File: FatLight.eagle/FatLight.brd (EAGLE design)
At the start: 75 x 100 mm, 27 parts, among them J1 12V, Q1 IRF540, Q2 IRF540, Q3 IRF540, Q4 16MHz, U1 ATMEGA328P-PU

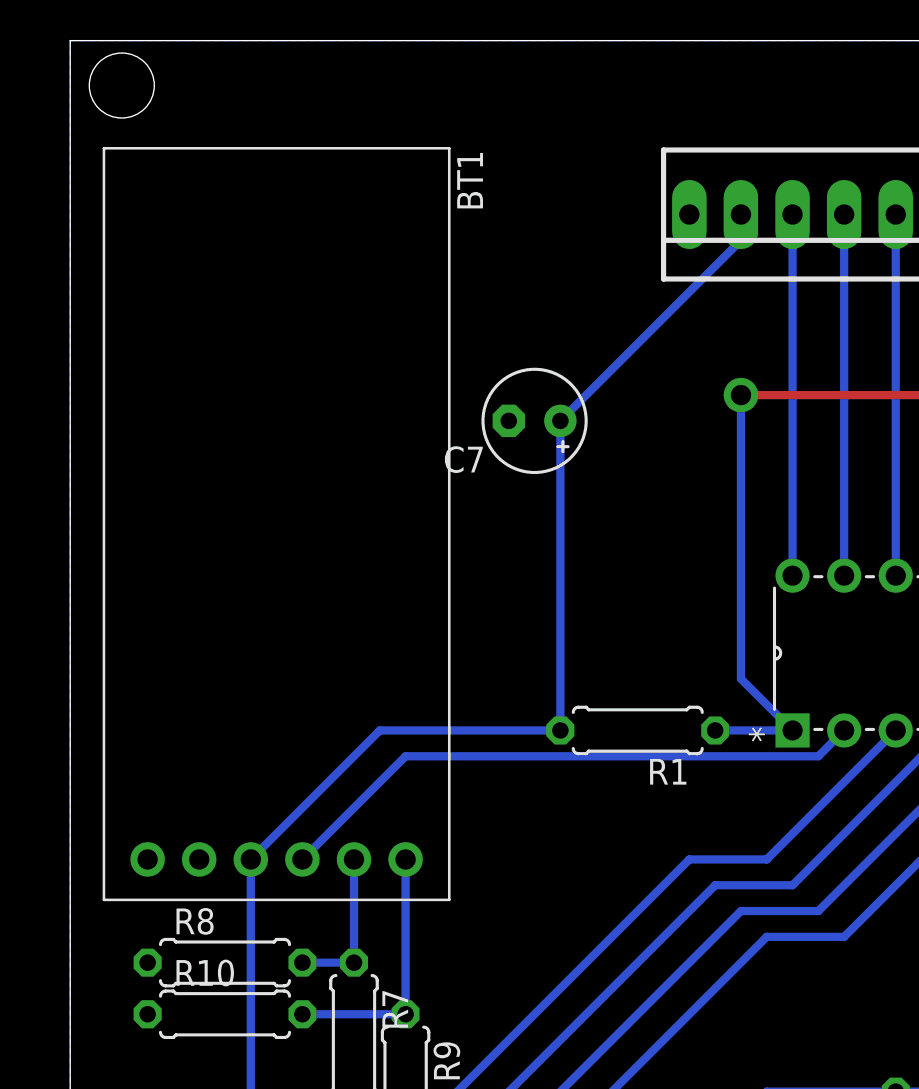
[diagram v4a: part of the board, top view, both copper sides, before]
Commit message: Updated Board and Schmeatics so either of two different HC-05 module types can be fitted. Bugfixes.
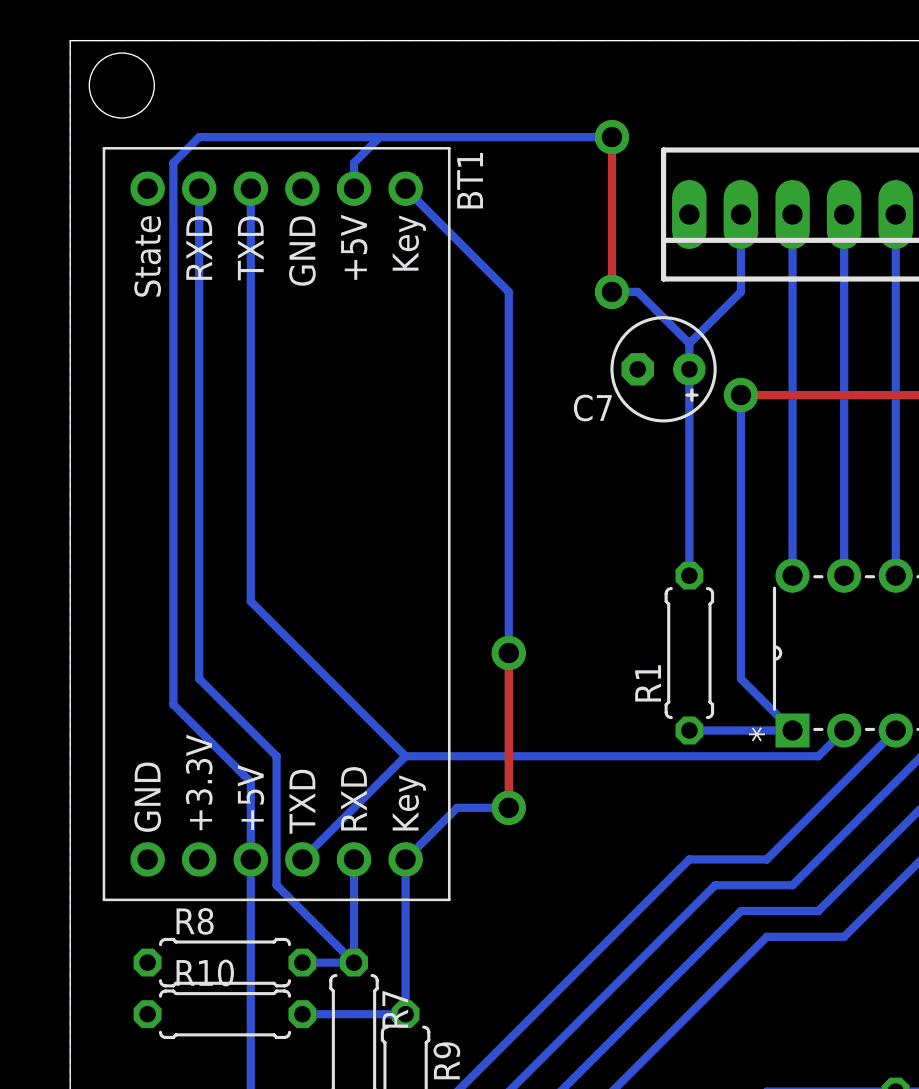
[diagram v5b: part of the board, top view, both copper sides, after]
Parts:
- moved C7 6.84 mm to (29.2, 83.8)
- moved R1 4.58 mm to (30.5, 69.8), turned to 90 degrees
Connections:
- net +5V: now also BT1.+5V1
- net GND: now also BT1.GND1
- net N$3: now also BT1.KEY1
- net N$4: now also BT1.RXD1
- net RXD_MCU: now also BT1.TXD1
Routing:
- net +5V: track 165.9 -> 211.3 mm, vias 0 -> 2
- net N$4: track 7.62 -> 48.9 mm
- net N$3: track 12.7 -> 51.4 mm, vias 0 -> 2
- net RXD_MCU: track 29.3 -> 60.4 mm
- net RESET: track 60.7 -> 62.0 mm
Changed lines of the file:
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@@
 <attribute name="OC_FARNELL" value="1667008" x="55.88" y="55.88" size="1.778" layer="27" rot="R90" display="off"/>
 </element>
-<element name="R1" library="rcl" package="0207/7" value="10k" x="27.94" y="66.04" rot="R180"/>
+<element name="R1" library="rcl" package="0207/7" value="10k" x="30.48" y="69.85" rot="R90"/>
 <element name="R10" library="rcl" package="0207/7" value="20k" x="7.62" y="52.07"/>
 <element name="R2" library="rcl" package="0207/7" value="10k" x="60.96" y="38.1" rot="R270"/>
@@
 <attribute name="OC_FARNELL" value="1715487" x="68.58" y="73.66" size="1.778" layer="27" rot="R90" display="off"/>
 </element>
-<element name="C7" library="rcl" package="E2,5-5" value="100µF" x="22.86" y="81.28" rot="R180"/>
+<element name="C7" library="rcl" package="E2,5-5" value="100µF" x="29.21" y="83.82" rot="R180"/>
 <element name="C8" library="rcl" package="C025-025X050" value="100nF" x="53.34" y="86.36" rot="R90"/>
 </elements>
@@
 <contactref element="C1" pad="2"/>
 <contactref element="C8" pad="2"/>
+<contactref element="BT1" pad="GND1"/>
 </signal>
 <signal name="+5V">
@@
 <wire x1="12.7" y1="41.91" x2="8.89" y2="45.72" width="0.4064" layer="16"/>
 <wire x1="8.89" y1="45.72" x2="8.89" y2="59.69" width="0.4064" layer="16"/>
-<wire x1="8.89" y1="59.69" x2="15.24" y2="66.04" width="0.4064" layer="16"/>
-<wire x1="15.24" y1="66.04" x2="24.13" y2="66.04" width="0.4064" layer="16"/>
 <wire x1="60.96" y1="91.44" x2="58.42" y2="91.44" width="0.4064" layer="16"/>
 <wire x1="58.42" y1="91.44" x2="55.88" y2="88.9" width="0.4064" layer="16"/>
 <wire x1="55.88" y1="88.9" x2="55.88" y2="78.74" width="0.4064" layer="16"/>
-<wire x1="24.13" y1="81.28" x2="24.13" y2="66.04" width="0.4064" layer="16"/>
+<wire x1="30.48" y1="83.82" x2="30.48" y2="73.66" width="0.4064" layer="16"/>
 <wire x1="15.24" y1="36.83" x2="15.24" y2="39.37" width="0.4064" layer="16"/>
 <wire x1="44.45" y1="64.77" x2="44.45" y2="67.31" width="0.4064" layer="16"/>
 <wire x1="44.45" y1="67.31" x2="46.99" y2="69.85" width="0.4064" layer="16"/>
 <wire x1="46.99" y1="69.85" x2="53.34" y2="69.85" width="0.4064" layer="16"/>
-<wire x1="33.02" y1="91.44" x2="33.02" y2="90.17" width="0.4064" layer="16"/>
-<wire x1="33.02" y1="90.17" x2="24.13" y2="81.28" width="0.4064" layer="16"/>
+<wire x1="30.48" y1="85.09" x2="30.48" y2="83.82" width="0.4064" layer="16"/>
 <wire x1="44.45" y1="64.77" x2="36.83" y2="57.15" width="0.4064" layer="16"/>
 <wire x1="36.83" y1="57.15" x2="33.02" y2="57.15" width="0.4064" layer="16"/>
@@
 <wire x1="33.02" y1="57.15" x2="15.24" y2="39.37" width="0.4064" layer="16"/>
 <contactref element="C7" pad="+"/>
+<contactref element="BT1" pad="+5V1"/>
+<wire x1="13.97" y1="92.71" x2="13.97" y2="93.98" width="0.4064" layer="16"/>
+<wire x1="13.97" y1="93.98" x2="15.24" y2="95.25" width="0.4064" layer="16"/>
+<wire x1="8.89" y1="59.69" x2="8.89" y2="63.5" width="0.4064" layer="16"/>
+<wire x1="8.89" y1="63.5" x2="5.08" y2="67.31" width="0.4064" layer="16"/>
+<wire x1="5.08" y1="67.31" x2="5.08" y2="93.98" width="0.4064" layer="16"/>
+<wire x1="5.08" y1="93.98" x2="6.35" y2="95.25" width="0.4064" layer="16"/>
+<wire x1="6.35" y1="95.25" x2="15.24" y2="95.25" width="0.4064" layer="16"/>
+<wire x1="33.02" y1="91.44" x2="33.02" y2="87.63" width="0.4064" layer="16"/>
+<wire x1="33.02" y1="87.63" x2="30.48" y2="85.09" width="0.4064" layer="16"/>
+<wire x1="15.24" y1="95.25" x2="26.67" y2="95.25" width="0.4064" layer="16"/>
+<via x="26.67" y="95.25" extent="1-16" drill="1"/>
+<wire x1="26.67" y1="95.25" x2="26.67" y2="87.63" width="0.4064" layer="1"/>
+<via x="26.67" y="87.63" extent="1-16" drill="1"/>
+<wire x1="26.67" y1="87.63" x2="27.94" y2="87.63" width="0.4064" layer="16"/>
+<wire x1="27.94" y1="87.63" x2="30.48" y2="85.09" width="0.4064" layer="16"/>
 </signal>
 <signal name="RESET">
@@
 <wire x1="33.02" y1="82.55" x2="33.02" y2="68.58" width="0.4064" layer="16"/>
 <wire x1="33.02" y1="68.58" x2="35.56" y2="66.04" width="0.4064" layer="16"/>
-<wire x1="35.56" y1="66.04" x2="31.75" y2="66.04" width="0.4064" layer="16"/>
+<wire x1="35.56" y1="66.04" x2="30.48" y2="66.04" width="0.4064" layer="16"/>
 </signal>
 <signal name="PWM_RED">
@@
 <wire x1="38.1" y1="66.04" x2="36.83" y2="64.77" width="0.4064" layer="16"/>
 <wire x1="36.83" y1="64.77" x2="16.51" y2="64.77" width="0.4064" layer="16"/>
+<contactref element="BT1" pad="TXD1"/>
+<wire x1="8.89" y1="92.71" x2="8.89" y2="72.39" width="0.4064" layer="16"/>
+<wire x1="8.89" y1="72.39" x2="16.51" y2="64.77" width="0.4064" layer="16"/>
 </signal>
 <signal name="TXD_MCU">
@@
 <wire x1="11.43" y1="52.07" x2="16.51" y2="52.07" width="0.4064" layer="16"/>
 <wire x1="16.51" y1="59.69" x2="16.51" y2="52.07" width="0.4064" layer="16"/>
+<contactref element="BT1" pad="KEY1"/>
+<wire x1="16.51" y1="59.69" x2="19.05" y2="62.23" width="0.4064" layer="16"/>
+<wire x1="19.05" y1="62.23" x2="21.59" y2="62.23" width="0.4064" layer="16"/>
+<via x="21.59" y="62.23" extent="1-16" drill="1"/>
+<wire x1="21.59" y1="62.23" x2="21.59" y2="69.85" width="0.4064" layer="1"/>
+<via x="21.59" y="69.85" extent="1-16" drill="1"/>
+<wire x1="21.59" y1="69.85" x2="21.59" y2="87.63" width="0.4064" layer="16"/>
+<wire x1="21.59" y1="87.63" x2="16.51" y2="92.71" width="0.4064" layer="16"/>
 </signal>
 <signal name="N$4">
@@
 <wire x1="11.43" y1="54.61" x2="13.97" y2="54.61" width="0.4064" layer="16"/>
 <wire x1="13.97" y1="59.69" x2="13.97" y2="54.61" width="0.4064" layer="16"/>
+<contactref element="BT1" pad="RXD1"/>
+<wire x1="6.35" y1="92.71" x2="6.35" y2="68.58" width="0.4064" layer="16"/>
+<wire x1="10.16" y1="64.77" x2="10.16" y2="58.42" width="0.4064" layer="16"/>
+<wire x1="10.16" y1="58.42" x2="13.97" y2="54.61" width="0.4064" layer="16"/>
+<wire x1="6.35" y1="68.58" x2="10.16" y2="64.77" width="0.4064" layer="16"/>
 </signal>
 <signal name="N$5">

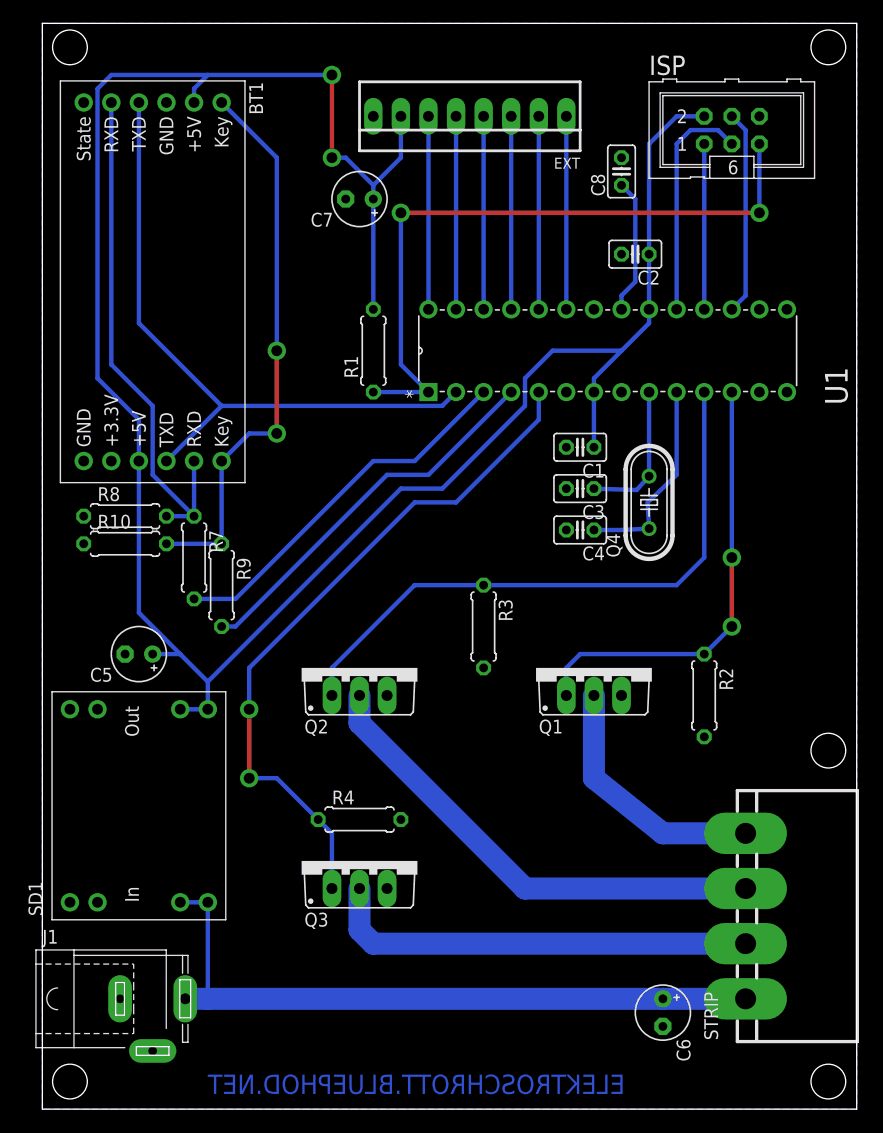
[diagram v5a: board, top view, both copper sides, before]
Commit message: Cap setting for random values added, optimized board layout.
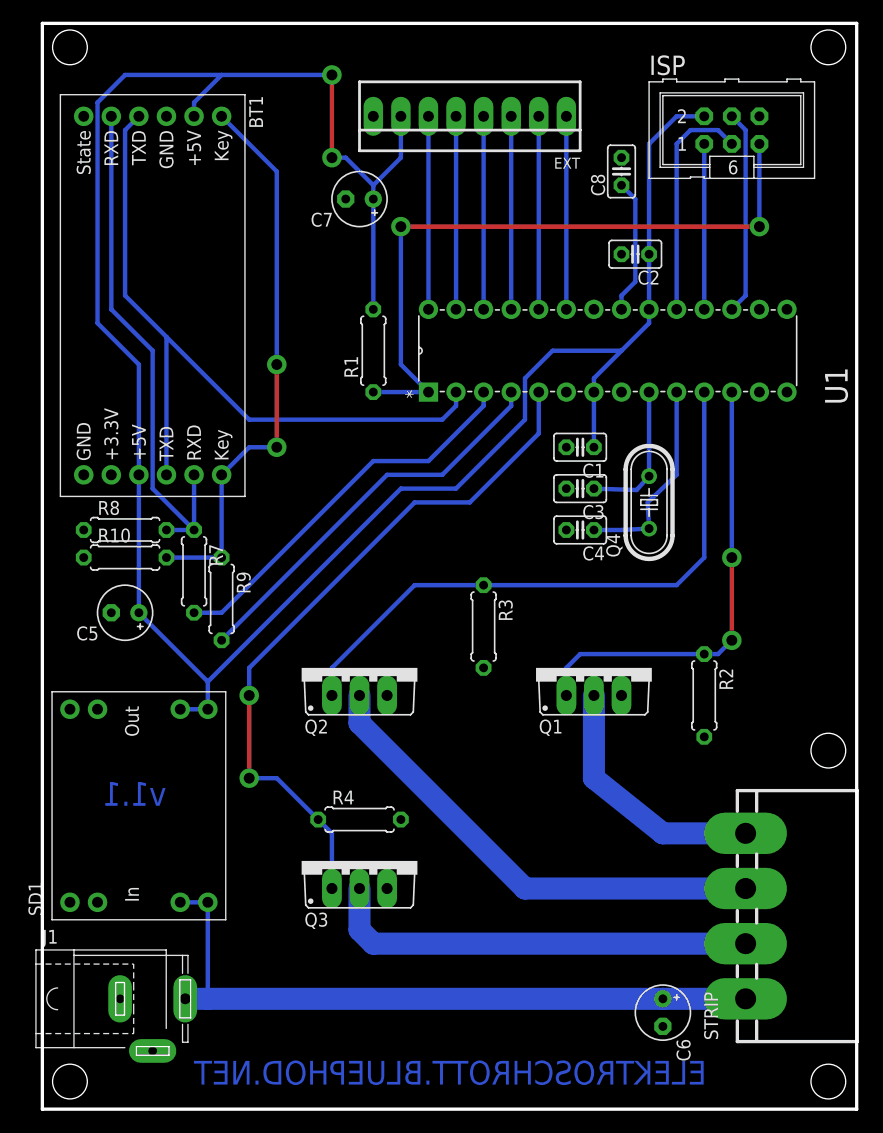
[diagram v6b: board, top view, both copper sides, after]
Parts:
- moved C5 4.02 mm to (7.62, 45.7)
- moved R10 1.27 mm to (7.62, 50.8)
- moved BT1 1.27 mm to (10.2, 74.9)
- moved R7 1.27 mm to (14.0, 49.5)
- moved R8 1.27 mm to (7.62, 53.3)
- moved R9 1.27 mm to (16.5, 47.0)
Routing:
- net RXD_MCU: track 60.4 -> 66.7 mm
- net TXD_MCU: track 34.6 -> 35.8 mm
- net KEY: track 35.6 -> 36.9 mm
- net +5V: track 211.3 -> 210.6 mm
- net PWM_RED: track 40.9 -> 41.7 mm
- net PWM_BLU: track 63.6 -> 64.4 mm
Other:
- board text added: "v1.1"

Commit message: Fixed the dimensions of the d-sun step-down module.
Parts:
- SD1: value STEP-DOWN -> D-SUN-STEPDOWN
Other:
- outline, holes or cut-outs redrawn
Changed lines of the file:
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@@
 <grid distance="0.05" unitdist="inch" unit="inch" style="lines" multiple="1" display="yes" altdistance="0.025" altunitdist="inch" altunit="inch"/>
 <layers>
-<layer number="1" name="Top" color="4" fill="1" visible="yes" active="yes"/>
+<layer number="1" name="Top" color="4" fill="1" visible="no" active="yes"/>
 <layer number="2" name="Route2" color="1" fill="3" visible="no" active="no"/>
 <layer number="3" name="Route3" color="4" fill="3" visible="no" active="no"/>
@@
 <layer number="17" name="Pads" color="2" fill="1" visible="yes" active="yes"/>
 <layer number="18" name="Vias" color="2" fill="1" visible="yes" active="yes"/>
-<layer number="19" name="Unrouted" color="6" fill="1" visible="yes" active="yes"/>
+<layer number="19" name="Unrouted" color="6" fill="1" visible="no" active="yes"/>
 <layer number="20" name="Dimension" color="15" fill="1" visible="yes" active="yes"/>
-<layer number="21" name="tPlace" color="7" fill="1" visible="yes" active="yes"/>
-<layer number="22" name="bPlace" color="7" fill="1" visible="yes" active="yes"/>
-<layer number="23" name="tOrigins" color="15" fill="1" visible="yes" active="yes"/>
-<layer number="24" name="bOrigins" color="15" fill="1" visible="yes" active="yes"/>
+<layer number="21" name="tPlace" color="7" fill="1" visible="no" active="yes"/>
+<layer number="22" name="bPlace" color="7" fill="1" visible="no" active="yes"/>
+<layer number="23" name="tOrigins" color="15" fill="1" visible="no" active="yes"/>
+<layer number="24" name="bOrigins" color="15" fill="1" visible="no" active="yes"/>
 <layer number="25" name="tNames" color="7" fill="1" visible="no" active="yes"/>
 <layer number="26" name="bNames" color="7" fill="1" visible="no" active="yes"/>
@@
 <layer number="46" name="Milling" color="3" fill="1" visible="no" active="yes"/>
 <layer number="47" name="Measures" color="7" fill="1" visible="no" active="yes"/>
-<layer number="48" name="Document" color="7" fill="1" visible="yes" active="yes"/>
+<layer number="48" name="Document" color="7" fill="1" visible="no" active="yes"/>
 <layer number="49" name="Reference" color="7" fill="1" visible="no" active="yes"/>
 <layer number="51" name="tDocu" color="7" fill="1" visible="no" active="yes"/>
@@
 <text x="13.97" y="4.445" size="2.1844" layer="16" rot="MR180">ELEKTROSCHROTT.BLUEPHOD.NET</text>
 <text x="11.43" y="27.94" size="2.1844" layer="16" rot="MR0">v1.1</text>
+<circle x="2.54" y="97.79" radius="1.6" width="0.127" layer="20"/>
+<circle x="72.39" y="97.79" radius="1.6" width="0.127" layer="20"/>
+<circle x="72.39" y="33.02" radius="1.6" width="0.127" layer="20"/>
+<circle x="72.39" y="2.54" radius="1.6" width="0.127" layer="20"/>
+<circle x="2.54" y="2.54" radius="1.6" width="0.127" layer="20"/>
 </plain>
 <attributes>
@@
 <param name="msMicroVia" value="9.99mm"/>
 <param name="msBlindViaRatio" value="0.5"/>
-<param name="rvPadTop" value="0.4"/>
-<param name="rvPadInner" value="0.4"/>
-<param name="rvPadBottom" value="0.4"/>
-<param name="rvViaOuter" value="0.4"/>
-<param name="rvViaInner" value="0.4"/>
+<param name="rvPadTop" value="0.36"/>
+<param name="rvPadInner" value="0.36"/>
+<param name="rvPadBottom" value="0.36"/>
+<param name="rvViaOuter" value="0.36"/>
+<param name="rvViaInner" value="0.36"/>
 <param name="rvMicroViaOuter" value="0.25"/>
 <param name="rvMicroViaInner" value="0.25"/>
@@
 <element name="R8" library="rcl" package="0207/7" value="20k" x="7.62" y="53.34"/>
 <element name="R9" library="rcl" package="0207/7" value="10k" x="16.51" y="46.99" rot="R270"/>
-<element name="SD1" library="Zap-Powerconverters" package="STEPDOWN-21X16" value="STEP-DOWN" x="8.89" y="27.94" rot="R90"/>
+<element name="SD1" library="Zap-Powerconverters" package="STEPDOWN-21X16" value="D-SUN-STEPDOWN" x="8.89" y="27.94" rot="R90"/>
 <element name="STRIP" library="con-amp" package="FLOP-4V" value="" x="64.77" y="17.78" rot="R90"/>
 <element name="U1" library="Zap-Mikrocontroller" package="DIP254P762X457-28" value="ATMEGA328P-PU" x="68.58" y="73.66" rot="R90">
@@
 <wire x1="50.8" y1="66.04" x2="50.8" y2="60.96" width="0.4064" layer="16"/>
 <contactref element="SD1" pad="OUT+1"/>
-<wire x1="12.7" y1="36.83" x2="15.24" y2="36.83" width="0.4064" layer="16"/>
+<wire x1="12.7" y1="37.19" x2="15.24" y2="37.19" width="0.4064" layer="16"/>
 <wire x1="55.88" y1="73.66" x2="55.88" y2="72.39" width="0.4064" layer="16"/>
 <wire x1="55.88" y1="72.39" x2="53.34" y2="69.85" width="0.4064" layer="16"/>
@@
 <wire x1="26.67" y1="87.63" x2="27.94" y2="87.63" width="0.4064" layer="16"/>
 <wire x1="27.94" y1="87.63" x2="30.48" y2="85.09" width="0.4064" layer="16"/>
-<wire x1="15.24" y1="36.83" x2="15.24" y2="39.37" width="0.4064" layer="16"/>
+<wire x1="15.24" y1="37.19" x2="15.24" y2="39.37" width="0.4064" layer="16"/>
 <wire x1="8.89" y1="45.72" x2="15.24" y2="39.37" width="0.4064" layer="16"/>
 </signal>
@@
 <contactref element="SD1" pad="IN+2"/>
 <wire x1="13.16" y1="10.16" x2="15.24" y2="10.16" width="2.032" layer="16"/>
-<wire x1="15.24" y1="19.05" x2="15.24" y2="10.16" width="0.4064" layer="16"/>
+<wire x1="15.24" y1="18.69" x2="15.24" y2="10.16" width="0.4064" layer="16"/>
 <wire x1="15.24" y1="10.16" x2="57.15" y2="10.16" width="2.032" layer="16"/>
 <contactref element="SD1" pad="IN+1"/>
 <wire x1="57.15" y1="10.16" x2="64.77" y2="10.16" width="2.032" layer="16"/>
-<wire x1="12.7" y1="19.05" x2="15.24" y2="19.05" width="0.4064" layer="16"/>
+<wire x1="12.7" y1="18.69" x2="15.24" y2="18.69" width="0.4064" layer="16"/>
 </signal>
 <signal name="N$3">
